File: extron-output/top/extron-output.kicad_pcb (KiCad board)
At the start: 2 copper layers, 99 x 65 mm, 14 parts, among them J1 SCART-F, J10 Conn_01x01, J11 RED2, J12 BLUE2, J13 SYNC2, J2 RED1, J3 GREEN, J4 BLUE1, J5 SYNC1, J6 PHOENIX, J8 Conn_01x01, J9 Conn_01x01, SW1 SW_SPDT

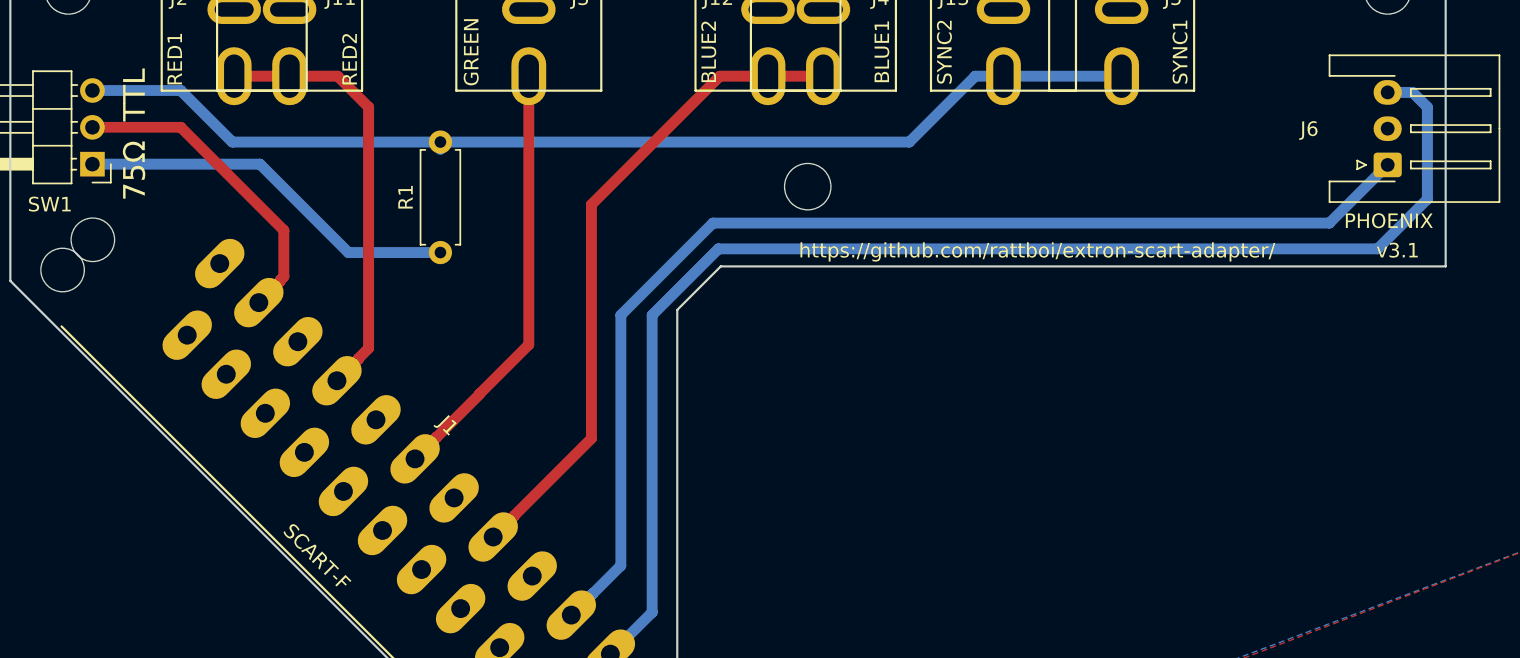
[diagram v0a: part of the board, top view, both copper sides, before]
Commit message: Update some images, move traces to make ground flood better
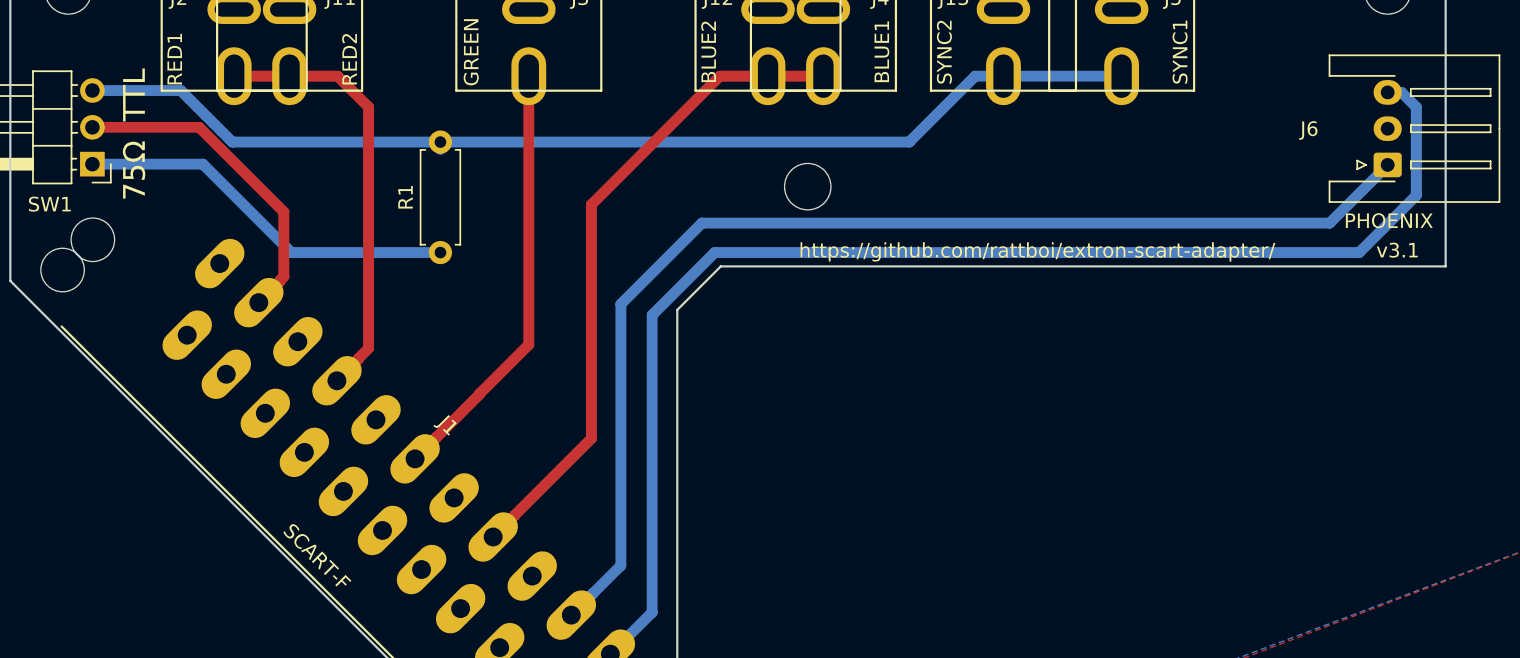
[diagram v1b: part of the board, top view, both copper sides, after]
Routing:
- net Net-(J1-Pad1): track 90.9 -> 89.2 mm
- net Net-(J1-Pad19): track 21.8 -> 22.6 mm
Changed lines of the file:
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@@
     (thickness 1.6)
     (drawings 12)
-    (tracks 52)
+    (tracks 53)
     (modules 14)
     (nets 10)
@@
   (segment (start 105.39948 110.790228) (end 105.39948 110.75452) (width 0.75) (layer "F.Cu") (net 4))
   (segment (start 128.26 85.88) (end 132.08 85.88) (width 0.75) (layer "F.Cu") (net 5))
-  (segment (start 173.736 94.361) (end 170.307 97.79) (width 0.75) (layer "B.Cu") (net 7))
-  (segment (start 173.736 88.011) (end 173.736 94.361) (width 0.75) (layer "B.Cu") (net 7))
-  (segment (start 170.307 97.79) (end 124.841 97.79) (width 0.75) (layer "B.Cu") (net 7))
-  (segment (start 171 87) (end 172.725 87) (width 0.75) (layer "B.Cu") (net 7))
-  (segment (start 172.725 87) (end 173.736 88.011) (width 0.75) (layer "B.Cu") (net 7))
-  (segment (start 120.269 102.362) (end 120.269 122.861477) (width 0.75) (layer "B.Cu") (net 7))
-  (segment (start 120.269 122.861477) (end 117.384941 125.745536) (width 0.75) (layer "B.Cu") (net 7))
-  (segment (start 124.841 97.79) (end 120.269 102.362) (width 0.75) (layer "B.Cu") (net 7))
-  (segment (start 124.46 96.012) (end 166.988 96.012) (width 0.75) (layer "B.Cu") (net 8))
-  (segment (start 166.988 96.012) (end 171 92) (width 0.75) (layer "B.Cu") (net 8))
-  (segment (start 118.11 102.362) (end 124.46 96.012) (width 0.75) (layer "B.Cu") (net 8))
-  (segment (start 118.11 119.634) (end 118.11 102.362) (width 0.75) (layer "B.Cu") (net 8))
-  (segment (start 116.177465 121.566535) (end 118.11 119.634) (width 0.75) (layer "B.Cu") (net 8))
-  (segment (start 114.690864 123.051459) (end 116.175788 121.566535) (width 0.75) (layer "B.Cu") (net 8))
-  (segment (start 116.175788 121.566535) (end 116.177465 121.566535) (width 0.75) (layer "B.Cu") (net 8))
   (segment (start 142.55 85.88) (end 144.5 85.88) (width 0.75) (layer "B.Cu") (net 3))
   (segment (start 138.006 90.424) (end 142.55 85.88) (width 0.75) (layer "B.Cu") (net 3))
@@
   (segment (start 81.661 86.868) (end 87.757 86.868) (width 0.75) (layer "B.Cu") (net 3))
   (segment (start 87.757 86.868) (end 91.313 90.424) (width 0.75) (layer "B.Cu") (net 3))
-  (segment (start 87.757 89.408) (end 81.661 89.408) (width 0.75) (layer "F.Cu") (net 6))
-  (segment (start 94.623173 100.01392) (end 94.623173 99.940827) (width 0.75) (layer "F.Cu") (net 6))
-  (segment (start 93.138249 101.498844) (end 94.623173 100.01392) (width 0.75) (layer "F.Cu") (net 6))
-  (segment (start 94.869 96.52) (end 87.757 89.408) (width 0.75) (layer "F.Cu") (net 6))
-  (segment (start 94.623173 99.940827) (end 94.869 99.695) (width 0.75) (layer "F.Cu") (net 6))
-  (segment (start 94.869 99.695) (end 94.869 96.52) (width 0.75) (layer "F.Cu") (net 6))
-  (segment (start 99.314 98.044) (end 105.664 98.044) (width 0.75) (layer "B.Cu") (net 9))
-  (segment (start 81.661 91.948) (end 93.218 91.948) (width 0.75) (layer "B.Cu") (net 9))
-  (segment (start 93.218 91.948) (end 99.314 98.044) (width 0.75) (layer "B.Cu") (net 9))
   (segment (start 100.011327 105.402074) (end 100.011327 105.347673) (width 0.75) (layer "F.Cu") (net 2))
   (segment (start 100.011327 105.347673) (end 100.711 104.648) (width 0.75) (layer "F.Cu") (net 2))
@@
   (segment (start 100.711 88.011) (end 98.58 85.88) (width 0.75) (layer "F.Cu") (net 2))
   (segment (start 100.711 104.648) (end 100.711 88.011) (width 0.75) (layer "F.Cu") (net 2))
+  (segment (start 89.027 89.408) (end 81.661 89.408) (width 0.75) (layer "F.Cu") (net 6))
+  (segment (start 94.623173 100.01392) (end 94.623173 99.940827) (width 0.75) (layer "F.Cu") (net 6))
+  (segment (start 94.869 95.25) (end 89.027 89.408) (width 0.75) (layer "F.Cu") (net 6))
+  (segment (start 93.138249 101.498844) (end 94.623173 100.01392) (width 0.75) (layer "F.Cu") (net 6))
+  (segment (start 94.623173 99.940827) (end 94.869 99.695) (width 0.75) (layer "F.Cu") (net 6))
+  (segment (start 94.869 99.695) (end 94.869 95.25) (width 0.75) (layer "F.Cu") (net 6))
+  (segment (start 95.377 98.044) (end 105.664 98.044) (width 0.75) (layer "B.Cu") (net 9))
+  (segment (start 81.661 91.948) (end 89.281 91.948) (width 0.75) (layer "B.Cu") (net 9))
+  (segment (start 89.281 91.948) (end 95.377 98.044) (width 0.75) (layer "B.Cu") (net 9))
+  (segment (start 120.269 122.861477) (end 117.384941 125.745536) (width 0.75) (layer "B.Cu") (net 7))
+  (segment (start 124.587 98.044) (end 120.269 102.362) (width 0.75) (layer "B.Cu") (net 7))
+  (segment (start 171.963 87) (end 172.974 88.011) (width 0.75) (layer "B.Cu") (net 7))
+  (segment (start 171 87) (end 171.963 87) (width 0.75) (layer "B.Cu") (net 7))
+  (segment (start 120.269 102.362) (end 120.269 122.861477) (width 0.75) (layer "B.Cu") (net 7))
+  (segment (start 172.974 88.011) (end 172.974 94.107) (width 0.75) (layer "B.Cu") (net 7))
+  (segment (start 172.974 94.107) (end 169.037 98.044) (width 0.75) (layer "B.Cu") (net 7))
+  (segment (start 169.037 98.044) (end 124.587 98.044) (width 0.75) (layer "B.Cu") (net 7))
+  (segment (start 167.005 96.012) (end 171 92.017) (width 0.75) (layer "B.Cu") (net 8))
+  (segment (start 123.698 96.012) (end 167.005 96.012) (width 0.75) (layer "B.Cu") (net 8))
+  (segment (start 116.175788 121.566535) (end 116.177465 121.566535) (width 0.75) (layer "B.Cu") (net 8))
+  (segment (start 114.690864 123.051459) (end 116.175788 121.566535) (width 0.75) (layer "B.Cu") (net 8))
+  (segment (start 171 92.017) (end 171 92) (width 0.75) (layer "B.Cu") (net 8))
+  (segment (start 118.11 119.634) (end 118.11 101.6) (width 0.75) (layer "B.Cu") (net 8))
+  (segment (start 116.177465 121.566535) (end 118.11 119.634) (width 0.75) (layer "B.Cu") (net 8))
+  (segment (start 118.11 101.6) (end 123.698 96.012) (width 0.75) (layer "B.Cu") (net 8))
   (zone (net 1) (net_name "GND") (layer "B.Cu") (hatch edge 0.508)
     (connect_pads (clearance 0.508))
